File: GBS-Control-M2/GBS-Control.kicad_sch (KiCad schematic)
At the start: 16 parts, among them J1 PROG, U1 PLCC-44 socket, U2 ESP-M2

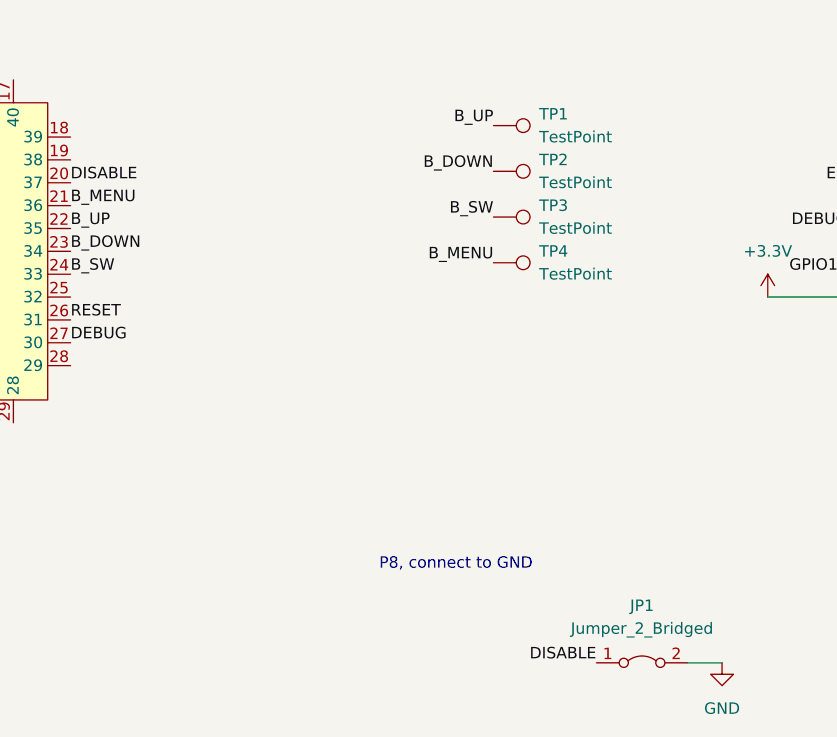
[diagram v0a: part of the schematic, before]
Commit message: KiCAD : add a port to connect the Si5351 Clock Generator
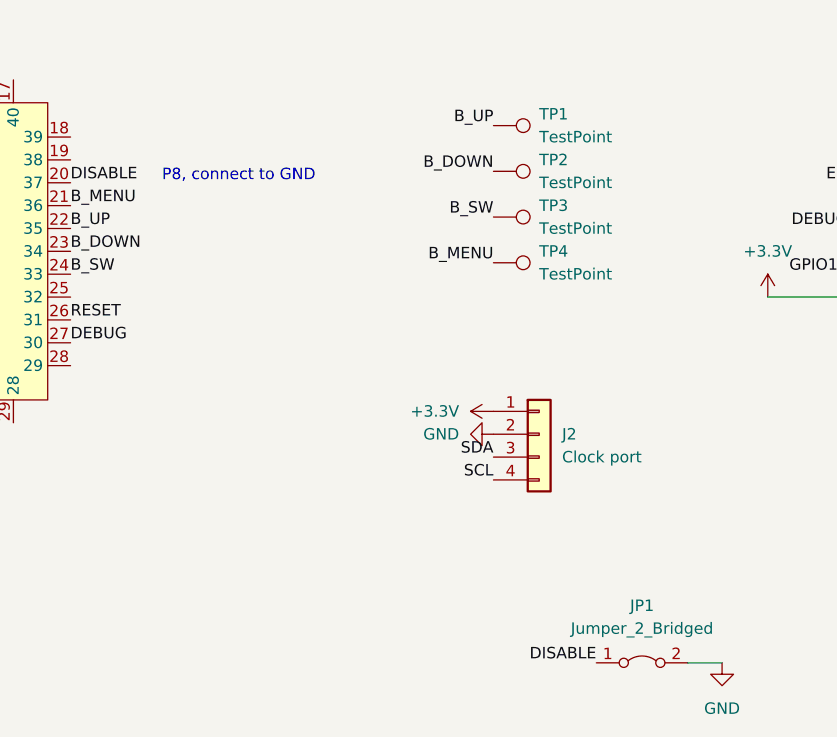
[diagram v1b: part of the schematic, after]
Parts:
- added J2: Clock port, Connector_PinHeader_2.54mm:PinHeader_1x04_P2.54mm_Vertical, symbol Connector_Generic:Conn_01x04
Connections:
- net +3.3V: now also J2.1 (Pin_1)
- net GND: now also J2.2 (Pin_2)
- net SCL: now also J2.4 (Pin_4)
- net SDA: now also J2.3 (Pin_3)
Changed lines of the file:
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@@
     (effects (font (size 1.27 1.27)) (justify left bottom))
   )
-  (text "P8, connect to GND" (at 140.97 133.35 0)
+  (text "P8, connect to GND" (at 116.84 90.17 0)
     (effects (font (size 1.27 1.27)) (justify left bottom))
   )
@@
     (effects (font (size 1.27 1.27)) (justify right bottom))
   )
+  (label "SDA" (at 153.67 120.65 180)
+    (effects (font (size 1.27 1.27)) (justify right bottom))
+  )
   (label "DISABLE" (at 106.68 90.17 0)
     (effects (font (size 1.27 1.27)) (justify left bottom))
@@
   )
   (label "EN" (at 257.81 77.47 180)
+    (effects (font (size 1.27 1.27)) (justify right bottom))
+  )
+  (label "SCL" (at 153.67 123.19 180)
     (effects (font (size 1.27 1.27)) (justify right bottom))
   )
@@
     )
     (property "Datasheet" "" (id 3) (at 179.07 143.51 0)
+      (effects (font (size 1.27 1.27)) hide)
+    )
+    (pin "1")
+  )
+  (symbol (lib_id "power:GND") (at 153.67 118.11 270) (unit 1)
+    (in_bom yes) (on_board yes) (fields_autoplaced)
+    (property "Reference" "#PWR011" (id 0) (at 147.32 118.11 0)
+      (effects (font (size 1.27 1.27)) hide)
+    )
+    (property "Value" "GND" (id 1) (at 149.86 118.1099 90)
+      (effects (font (size 1.27 1.27)) (justify right))
+    )
+    (property "Footprint" "" (id 2) (at 153.67 118.11 0)
+      (effects (font (size 1.27 1.27)) hide)
+    )
+    (property "Datasheet" "" (id 3) (at 153.67 118.11 0)
       (effects (font (size 1.27 1.27)) hide)
     )
@@
     (pin "1")
   )
+  (symbol (lib_id "Connector_Generic:Conn_01x04") (at 158.75 118.11 0) (unit 1)
+    (in_bom yes) (on_board yes) (fields_autoplaced)
+    (property "Reference" "J2" (id 0) (at 161.29 118.1099 0)
+      (effects (font (size 1.27 1.27)) (justify left))
+    )
+    (property "Value" "Clock port" (id 1) (at 161.29 120.6499 0)
+      (effects (font (size 1.27 1.27)) (justify left))
+    )
+    (property "Footprint" "Connector_PinHeader_2.54mm:PinHeader_1x04_P2.54mm_Vertical" (id 2) (at 158.75 118.11 0)
+      (effects (font (size 1.27 1.27)) hide)
+    )
+    (property "Datasheet" "~" (id 3) (at 158.75 118.11 0)
+      (effects (font (size 1.27 1.27)) hide)
+    )
+    (pin "1")
+    (pin "2")
+    (pin "3")
+    (pin "4")
+  )
   (symbol (lib_id "Device:R_Small") (at 250.19 54.61 0) (unit 1)
     (in_bom yes) (on_board yes) (fields_autoplaced)
@@
     (pin "1")
     (pin "2")
+  )
+  (symbol (lib_id "power:+3.3V") (at 153.67 115.57 90) (unit 1)
+    (in_bom yes) (on_board yes) (fields_autoplaced)
+    (property "Reference" "#PWR010" (id 0) (at 157.48 115.57 0)
+      (effects (font (size 1.27 1.27)) hide)
+    )
+    (property "Value" "+3.3V" (id 1) (at 149.86 115.5699 90)
+      (effects (font (size 1.27 1.27)) (justify left))
+    )
+    (property "Footprint" "" (id 2) (at 153.67 115.57 0)
+      (effects (font (size 1.27 1.27)) hide)
+    )
+    (property "Datasheet" "" (id 3) (at 153.67 115.57 0)
+      (effects (font (size 1.27 1.27)) hide)
+    )
+    (pin "1")
   )
   (symbol (lib_id "Device:C_Small") (at 205.74 54.61 0) (unit 1)
@@
       (reference "#PWR09") (unit 1) (value "GND") (footprint "")
     )
+    (path "/ea3b2351-20bb-45c5-904e-79a063ddbe65"
+      (reference "#PWR010") (unit 1) (value "+3.3V") (footprint "")
+    )
+    (path "/31a6a935-5069-4fb5-992b-a18fef0e6257"
+      (reference "#PWR011") (unit 1) (value "GND") (footprint "")
+    )
     (path "/de315ed7-c989-4a04-a0b0-f4d9be38c2a0"
       (reference "#PWR0101") (unit 1) (value "+3.3V") (footprint "")
@@
       (reference "J1") (unit 1) (value "PROG") (footprint "Connector_PinSocket_2.54mm:PinSocket_1x06_P2.54mm_Vertical")
     )
+    (path "/b62abfb6-5e6a-4457-b183-1c8d22d7caa6"
+      (reference "J2") (unit 1) (value "Clock port") (footprint "Connector_PinHeader_2.54mm:PinHeader_1x04_P2.54mm_Vertical")
+    )
     (path "/54c5d063-2856-40e7-ba64-3c2e09206442"

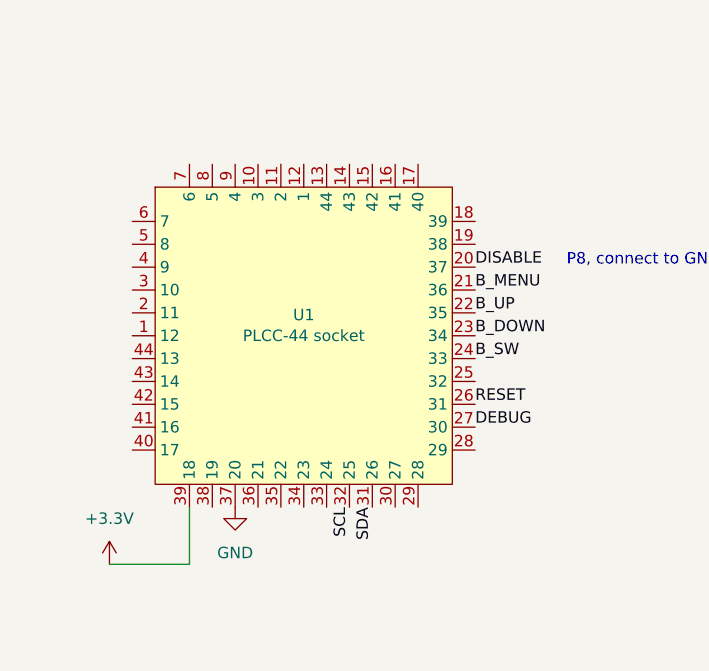
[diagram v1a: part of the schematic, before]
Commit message: GBS-Control-12F, GBS-Control-M2 : update socket symbol and footprint, no PCB change
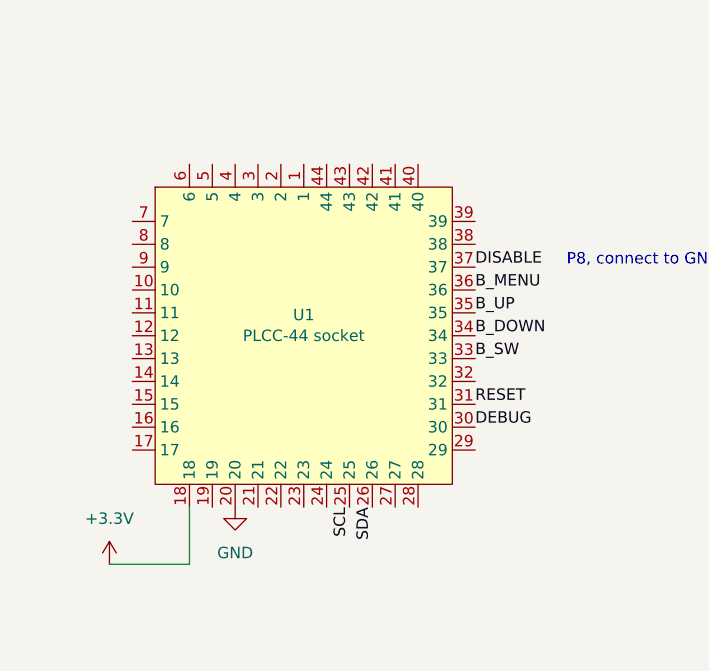
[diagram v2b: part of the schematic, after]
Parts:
- U1: footprint Package_LCC:PLCC-44_THT-Socket -> Sassa:PLCC-44_THT-SocketOnTop; symbol Sassa:PLCC-44_Socket-on-top -> Sassa:PLCC-44
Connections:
- net +3.3V: now also U1.18; no longer U1.39 (18)
- net B_DOWN: now also U1.34; no longer U1.23 (34)
- net B_MENU: now also U1.36; no longer U1.21 (36)
- net B_SW: now also U1.33; no longer U1.24 (33)
- net B_UP: now also U1.35; no longer U1.22 (35)
- net DEBUG: now also U1.30; no longer U1.27 (30)
- net DISABLE: now also U1.37; no longer U1.20 (37)
- net GND: now also U1.20; no longer U1.37 (20)
- net RESET: now also U1.31; no longer U1.26 (31)
- net SCL: now also U1.25; no longer U1.32 (25)
- net SDA: now also U1.26; no longer U1.31 (26)
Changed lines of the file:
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@@
     (pin "2")
   )
-  (symbol (lib_id "Sassa:PLCC-44_Socket-on-top") (at 87.63 97.79 0) (unit 1)
+  (symbol (lib_id "Sassa:PLCC-44") (at 87.63 97.79 0) (unit 1)
     (in_bom yes) (on_board yes)
     (property "Reference" "U1" (id 0) (at 87.63 95.4786 0))
     (property "Value" "PLCC-44 socket" (id 1) (at 87.63 97.79 0))
-    (property "Footprint" "Package_LCC:PLCC-44_THT-Socket" (id 2) (at 87.63 97.79 0)
+    (property "Footprint" "Sassa:PLCC-44_THT-SocketOnTop" (id 2) (at 87.63 97.79 0)
       (effects (font (size 1.27 1.27)) hide)
     )
@@
     )
     (path "/f402a2e4-184a-49e9-9b5a-85c4ce735b3e"
-      (reference "U1") (unit 1) (value "PLCC-44 socket") (footprint "Package_LCC:PLCC-44_THT-Socket")
+      (reference "U1") (unit 1) (value "PLCC-44 socket") (footprint "Sassa:PLCC-44_THT-SocketOnTop")
     )
     (path "/96f3aece-9725-4b35-9e19-545ba8ef3878"
